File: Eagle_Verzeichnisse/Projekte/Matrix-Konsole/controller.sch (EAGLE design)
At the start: 20 parts, among them IC1 74HC165D

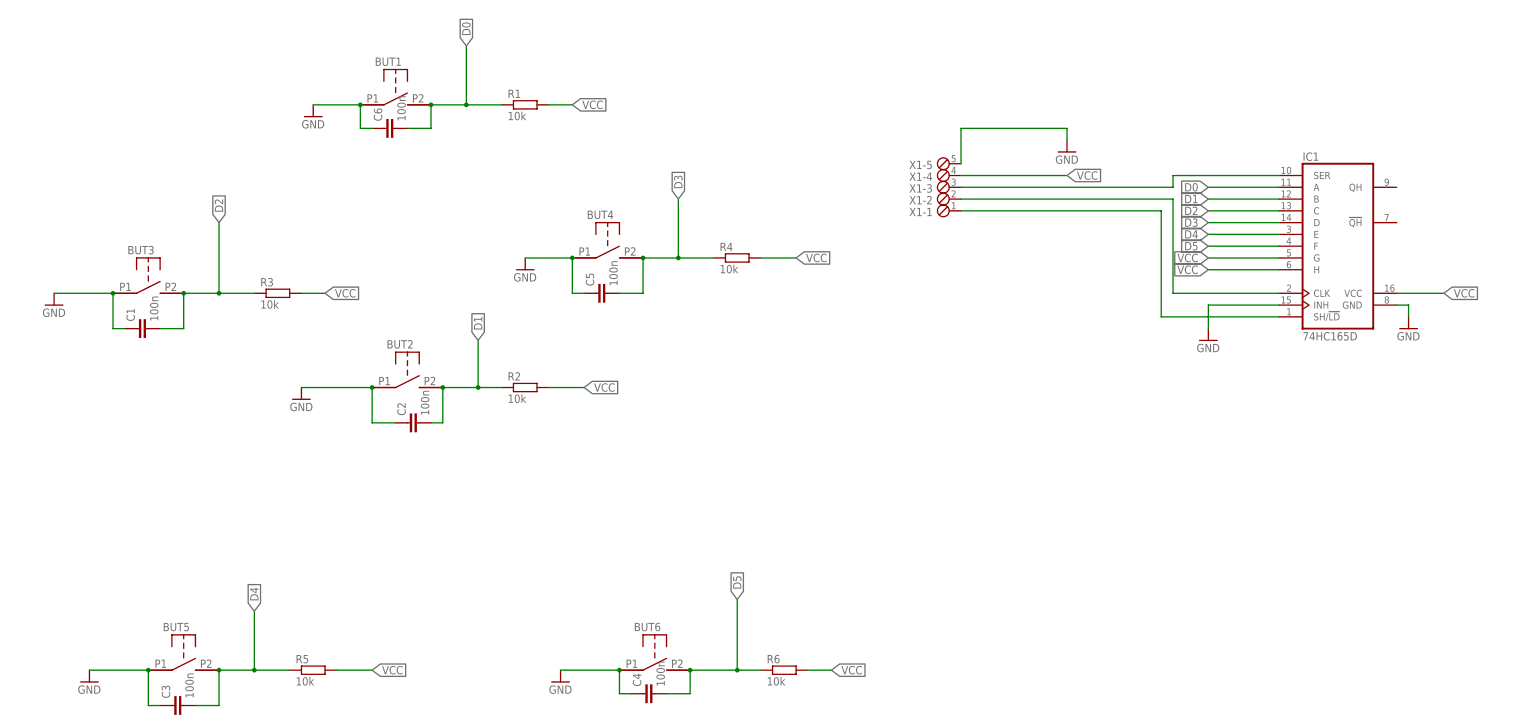
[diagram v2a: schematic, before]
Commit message: Added Z-Diode
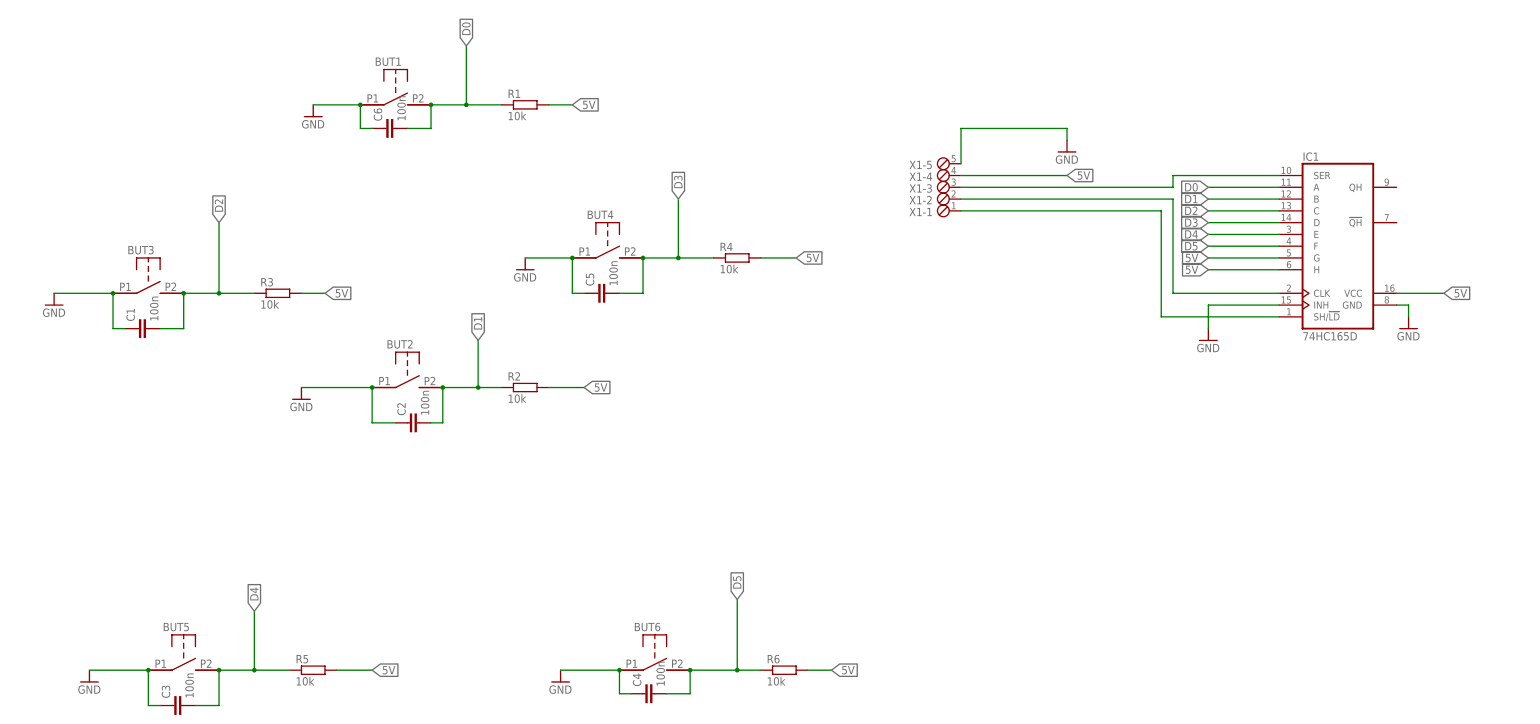
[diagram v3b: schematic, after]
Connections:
- net VCC renamed 5V
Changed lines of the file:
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@@
 <setting verticaltext="up"/>
 </settings>
-<grid distance="0.1" unitdist="inch" unit="inch" style="lines" multiple="1" display="no" altdistance="0.01" altunitdist="inch" altunit="inch"/>
+<grid distance="0.1" unitdist="inch" unit="inch" style="lines" multiple="1" display="yes" altdistance="0.01" altunitdist="inch" altunit="inch"/>
 <layers>
 <layer number="1" name="Top" color="4" fill="1" visible="no" active="no"/>
@@
 </segment>
 </net>
-<net name="VCC" class="0">
-<segment>
-<pinref part="IC1" gate="A" pin="VCC"/>
-<wire x1="35.56" y1="33.02" x2="45.72" y2="33.02" width="0.1524" layer="91"/>
-<label x="45.72" y="33.02" size="1.778" layer="95" xref="yes"/>
-</segment>
-<segment>
-<pinref part="X1" gate="-4" pin="1"/>
-<wire x1="-58.42" y1="58.42" x2="-35.56" y2="58.42" width="0.1524" layer="91"/>
-<label x="-35.56" y="58.42" size="1.778" layer="95" xref="yes"/>
-</segment>
-<segment>
-<pinref part="IC1" gate="A" pin="G"/>
-<wire x1="10.16" y1="40.64" x2="-5.08" y2="40.64" width="0.1524" layer="91"/>
-<label x="-5.08" y="40.64" size="1.778" layer="95" rot="R180" xref="yes"/>
-</segment>
-<segment>
-<pinref part="IC1" gate="A" pin="H"/>
-<wire x1="10.16" y1="38.1" x2="-5.08" y2="38.1" width="0.1524" layer="91"/>
-<label x="-5.08" y="38.1" size="1.778" layer="95" rot="R180" xref="yes"/>
-</segment>
-<segment>
-<wire x1="-147.32" y1="73.66" x2="-142.24" y2="73.66" width="0.1524" layer="91"/>
-<label x="-142.24" y="73.66" size="1.778" layer="95" xref="yes"/>
-<pinref part="R1" gate="G$1" pin="2"/>
-</segment>
-<segment>
-<wire x1="-101.6" y1="40.64" x2="-93.98" y2="40.64" width="0.1524" layer="91"/>
-<label x="-93.98" y="40.64" size="1.778" layer="95" xref="yes"/>
-<pinref part="R4" gate="G$1" pin="2"/>
-</segment>
-<segment>
-<wire x1="-147.32" y1="12.7" x2="-139.7" y2="12.7" width="0.1524" layer="91"/>
-<label x="-139.7" y="12.7" size="1.778" layer="95" xref="yes"/>
-<pinref part="R2" gate="G$1" pin="2"/>
-</segment>
-<segment>
-<wire x1="-200.66" y1="33.02" x2="-195.58" y2="33.02" width="0.1524" layer="91"/>
-<label x="-195.58" y="33.02" size="1.778" layer="95" xref="yes"/>
-<pinref part="R3" gate="G$1" pin="2"/>
-</segment>
-<segment>
-<wire x1="-193.04" y1="-48.26" x2="-185.42" y2="-48.26" width="0.1524" layer="91"/>
-<label x="-185.42" y="-48.26" size="1.778" layer="95" xref="yes"/>
-<pinref part="R5" gate="G$1" pin="2"/>
-</segment>
-<segment>
-<wire x1="-91.44" y1="-48.26" x2="-86.36" y2="-48.26" width="0.1524" layer="91"/>
-<label x="-86.36" y="-48.26" size="1.778" layer="95" xref="yes"/>
-<pinref part="R6" gate="G$1" pin="2"/>
-</segment>
-</net>
 <net name="D0" class="0">
 <segment>
@@
 </segment>
 </net>
+<net name="5V" class="0">
+<segment>
+<wire x1="-147.32" y1="73.66" x2="-142.24" y2="73.66" width="0.1524" layer="91"/>
+<label x="-142.24" y="73.66" size="1.778" layer="95" xref="yes"/>
+<pinref part="R1" gate="G$1" pin="2"/>
+</segment>
+<segment>
+<wire x1="-101.6" y1="40.64" x2="-93.98" y2="40.64" width="0.1524" layer="91"/>
+<label x="-93.98" y="40.64" size="1.778" layer="95" xref="yes"/>
+<pinref part="R4" gate="G$1" pin="2"/>
+</segment>
+<segment>
+<wire x1="-147.32" y1="12.7" x2="-139.7" y2="12.7" width="0.1524" layer="91"/>
+<label x="-139.7" y="12.7" size="1.778" layer="95" xref="yes"/>
+<pinref part="R2" gate="G$1" pin="2"/>
+</segment>
+<segment>
+<wire x1="-200.66" y1="33.02" x2="-195.58" y2="33.02" width="0.1524" layer="91"/>
+<label x="-195.58" y="33.02" size="1.778" layer="95" xref="yes"/>
+<pinref part="R3" gate="G$1" pin="2"/>
+</segment>
+<segment>
+<pinref part="X1" gate="-4" pin="1"/>
+<wire x1="-58.42" y1="58.42" x2="-35.56" y2="58.42" width="0.1524" layer="91"/>
+<label x="-35.56" y="58.42" size="1.778" layer="95" xref="yes"/>
+</segment>
+<segment>
+<pinref part="IC1" gate="A" pin="H"/>
+<wire x1="10.16" y1="38.1" x2="-5.08" y2="38.1" width="0.1524" layer="91"/>
+<label x="-5.08" y="38.1" size="1.778" layer="95" rot="R180" xref="yes"/>
+</segment>
+<segment>
+<pinref part="IC1" gate="A" pin="G"/>
+<wire x1="10.16" y1="40.64" x2="-5.08" y2="40.64" width="0.1524" layer="91"/>
+<label x="-5.08" y="40.64" size="1.778" layer="95" rot="R180" xref="yes"/>
+</segment>
+<segment>
+<pinref part="IC1" gate="A" pin="VCC"/>
+<wire x1="35.56" y1="33.02" x2="45.72" y2="33.02" width="0.1524" layer="91"/>
+<label x="45.72" y="33.02" size="1.778" layer="95" xref="yes"/>
+</segment>
+<segment>
+<wire x1="-91.44" y1="-48.26" x2="-86.36" y2="-48.26" width="0.1524" layer="91"/>
+<label x="-86.36" y="-48.26" size="1.778" layer="95" xref="yes"/>
+<pinref part="R6" gate="G$1" pin="2"/>
+</segment>
+<segment>
+<wire x1="-193.04" y1="-48.26" x2="-185.42" y2="-48.26" width="0.1524" layer="91"/>
+<label x="-185.42" y="-48.26" size="1.778" layer="95" xref="yes"/>
+<pinref part="R5" gate="G$1" pin="2"/>
+</segment>
+</net>

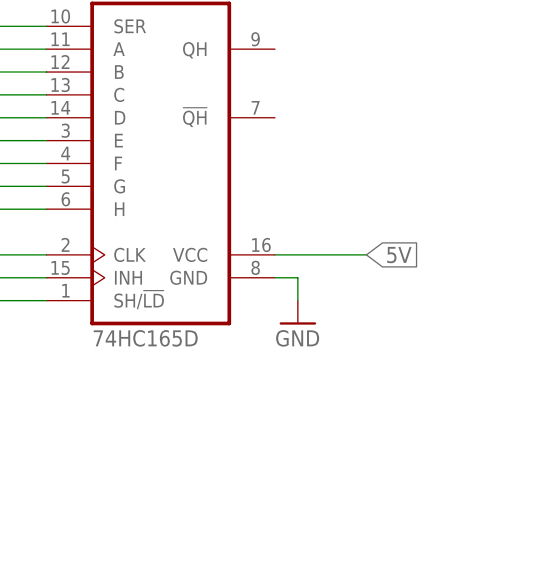
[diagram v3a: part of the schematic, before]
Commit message: Added Layout for console
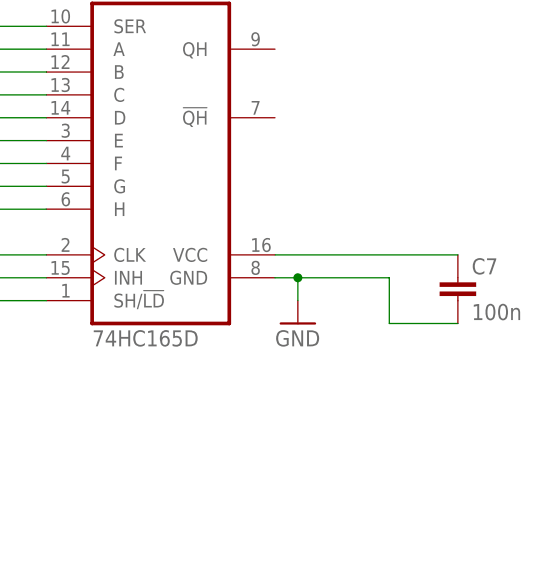
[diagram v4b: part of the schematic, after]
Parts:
- added C7: 100n, eagle-ltspice:C
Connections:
- net 5V: now also C7.1
- net GND: now also C7.2
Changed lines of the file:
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@@
 <part name="R5" library="resistor" deviceset="R-EU_" device="M3516" value="10k"/>
 <part name="R6" library="resistor" deviceset="R-EU_" device="M3516" value="10k"/>
+<part name="C7" library="eagle-ltspice" deviceset="C" device="" value="100n"/>
 </parts>
 <sheets>
@@
 <instance part="R5" gate="G$1" x="-198.12" y="-48.26"/>
 <instance part="R6" gate="G$1" x="-96.52" y="-48.26"/>
+<instance part="C7" gate="G$1" x="55.88" y="30.48"/>
 </instances>
 <busses>
@@
 <wire x1="35.56" y1="30.48" x2="38.1" y2="30.48" width="0.1524" layer="91"/>
 <wire x1="38.1" y1="30.48" x2="38.1" y2="27.94" width="0.1524" layer="91"/>
+<wire x1="38.1" y1="30.48" x2="48.26" y2="30.48" width="0.1524" layer="91"/>
+<wire x1="48.26" y1="30.48" x2="48.26" y2="25.4" width="0.1524" layer="91"/>
+<junction x="38.1" y="30.48"/>
+<pinref part="C7" gate="G$1" pin="2"/>
+<wire x1="48.26" y1="25.4" x2="55.88" y2="25.4" width="0.1524" layer="91"/>
 </segment>
 <segment>
@@
 <segment>
 <pinref part="IC1" gate="A" pin="VCC"/>
-<wire x1="35.56" y1="33.02" x2="45.72" y2="33.02" width="0.1524" layer="91"/>
-<label x="45.72" y="33.02" size="1.778" layer="95" xref="yes"/>
-</segment>
-<segment>
+<pinref part="C7" gate="G$1" pin="1"/>
+<wire x1="35.56" y1="33.02" x2="55.88" y2="33.02" width="0.1524" layer="91"/>
+</segment>
+<segment>
